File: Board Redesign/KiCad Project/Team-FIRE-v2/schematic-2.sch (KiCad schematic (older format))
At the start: 20 parts, among them J4 Conn_01x03, J5 Conn_ARM_JTAG_SWD_10, U4 TXB0108DQSR, U7 TXB0104RUT

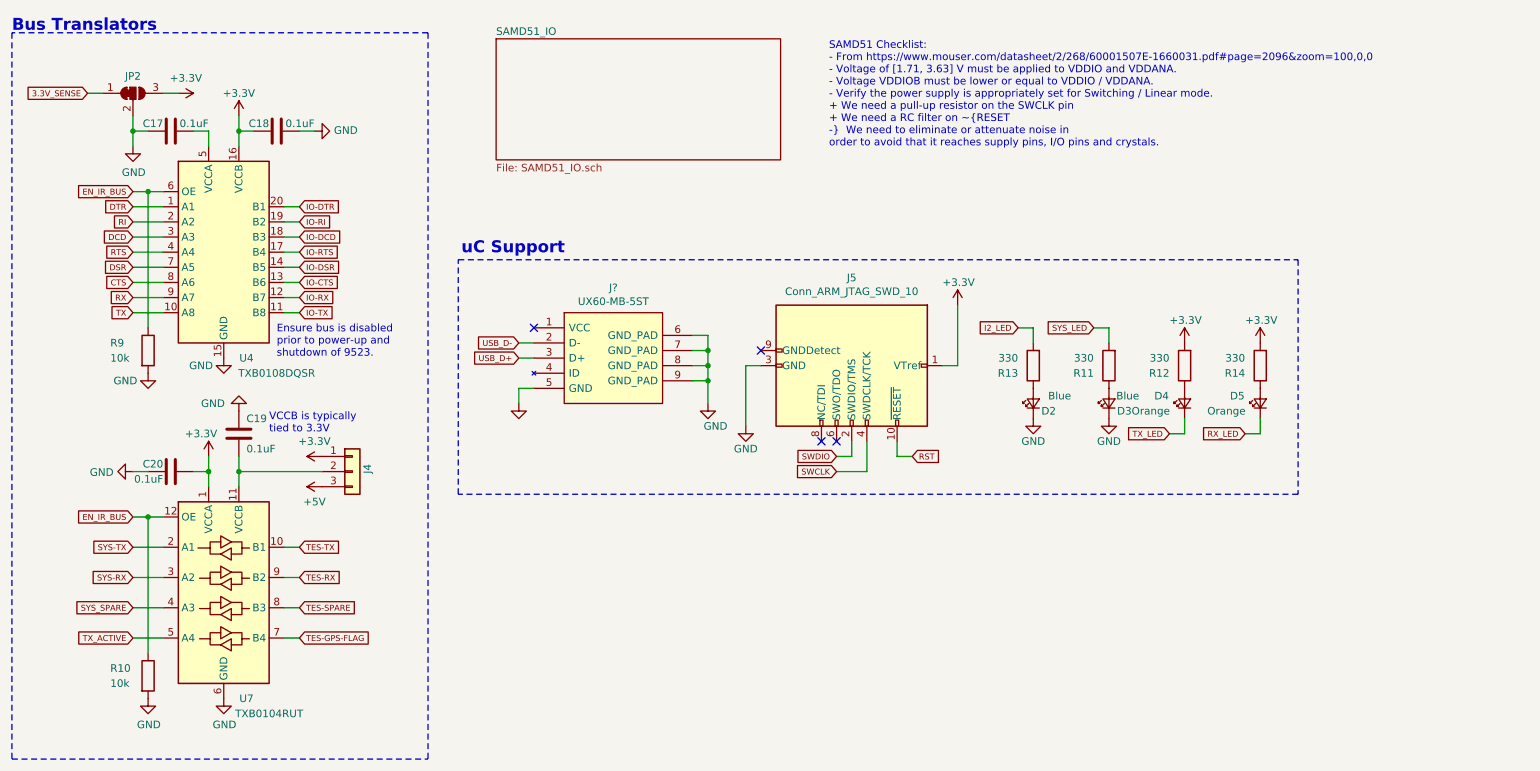
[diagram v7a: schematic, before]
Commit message: Labelled finished sections on schematic, picked LEDs
- Labelled all finished schematic sections if they've been part-selected / verified (and by whom)
- Selected the four debug LEDs and filled out BOM info
- Filled out info for Power/TES connectors
- Filled out info for RF connector
- Filled out info for 5 to 3.3V regulator
- Filled out info for 8 to 5V switching regulator
- Assigned footprints to test points
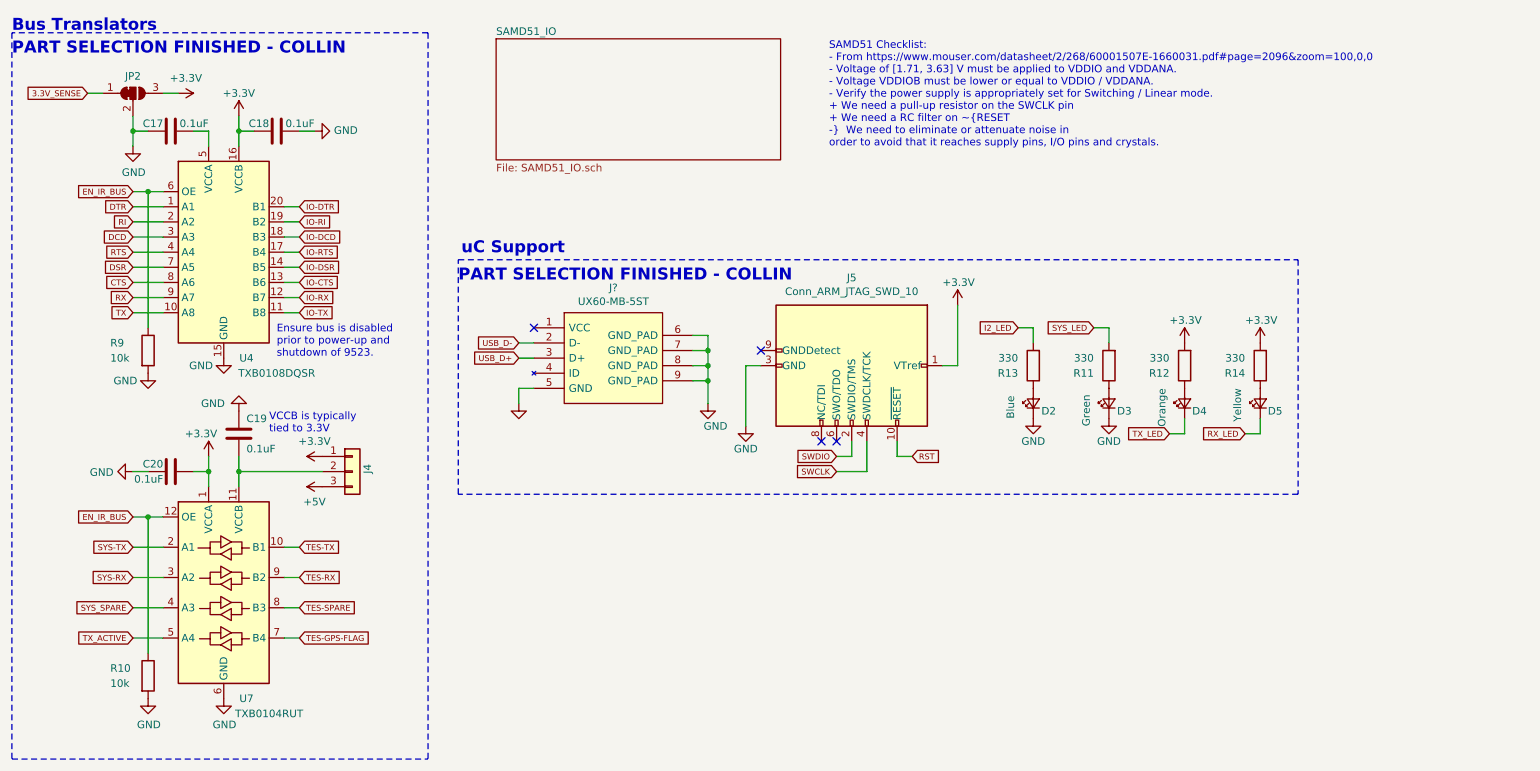
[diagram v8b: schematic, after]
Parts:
- D2: footprint (none) -> LED_SMD:LED_0603_1608Metric; Description (none) -> Blue I2 LED; Link (none) -> https://www.mouser.com/ProductDetail/OSRAM-Opto-Semiconduct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; MPN (none) -> KB DELPS2.12-QHRI-24-Z555-10-S; Manufacturer (none) -> Osram Opto Semiconductor; Supplier (none) -> Mouser; Supplier PN (none) -> 720-KBDELPS212A6350
- D3: value Blue -> Green; footprint (none) -> LED_SMD:LED_0603_1608Metric; Description (none) -> Green SYS LED; Link (none) -> https://www.mouser.com/ProductDetail/OSRAM-Opto-Semiconduct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; MPN (none) -> KG DELMS1.22-PHQI-24-E6L6; Manufacturer (none) -> Osram Opto Semiconductor; Supplier (none) -> Mouser; Supplier PN (none) -> 720-KGDELMS122A4854
- D4: footprint (none) -> LED_SMD:LED_0603_1608Metric; Description (none) -> Orange TX LED; Link (none) -> https://www.mouser.com/ProductDetail/OSRAM-Opto-Semiconduct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; MPN (none) -> KO DELLS1.22-KHLI-24; Manufacturer (none) -> Osram Opto Semiconductor; Supplier (none) -> Mouser; Supplier PN (none) -> 720-KODELLS122A4850
- D5: value Orange -> Yellow; footprint (none) -> LED_SMD:LED_0603_1608Metric; Description (none) -> Yellow RX LED; Link (none) -> https://www.mouser.com/ProductDetail/OSRAM-Opto-Semiconduct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; MPN (none) -> KY DELLS1.22-KGLH-26; Manufacturer (none) -> Osram Opto Semiconductor; Supplier (none) -> Mouser; Supplier PN (none) -> 720-KYDELLS122A4853
- J5: footprint (none) -> Connector_PinHeader_1.27mm:PinHeader_2x05_P1.27mm_Vertical_SMD; Current Rating (none) -> 3.4 A per contact; Desription (none) -> JTAG connector; Link (none) -> https://www.digikey.ca/product-detail/en/samtec-inc/FTSH-10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; MPN (none) -> FTSH-105-01-L-DV-K-TR; Manufacturer (none) -> Samtec Inc.; Supplier (none) -> Digikey; Supplier PN (none) -> SAM13165CT-ND
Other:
- note added: "PART SELECTION FINISHED - COLLIN"
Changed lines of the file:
@@
 P 7350 3150
 F 0 "D2" V 7300 3000 50  0000 L CNN
-F 1 "Blue" V 7400 2900 50  0000 L CNN
-F 2 "" V 7350 3150 50  0001 C CNN
-F 3 "~" V 7350 3150 50  0001 C CNN
+F 1 "Blue" H 7250 3300 50  0000 L CNN
+F 2 "LED_SMD:LED_0603_1608Metric" V 7350 3150 50  0001 C CNN
+F 3 "https://dammedia.osram.info/media/resource/hires/osram-dam-5455914/KB%20DELPS2.12_EN.pdf" V 7350 3150 50  0001 C CNN
+F 4 "KB DELPS2.12-QHRI-24-Z555-10-S" V 7350 3150 50  0001 C CNN "MPN"
+F 5 "Osram Opto Semiconductor" V 7350 3150 50  0001 C CNN "Manufacturer"
+F 6 "Mouser" V 7350 3150 50  0001 C CNN "Supplier"
+F 7 "720-KBDELPS212A6350" V 7350 3150 50  0001 C CNN "Supplier PN"
+F 8 "https://www.mouser.com/ProductDetail/OSRAM-Opto-Semiconductors/KB-DELPS212-QHRI-24-Z555-10-S?qs=sGAEpiMZZMseGfSY3csMkXiJOH5X%252BfXwwcjMMWonTAhZIqH765egag%3D%3D" V 7350 3150 50  0001 C CNN "Link"
+F 9 "Blue I2 LED" V 7350 3150 50  0001 C CNN "Description"
 	1    7350 3150
 	0    -1   -1   0
@@
 P 7850 3150
 F 0 "D3" V 7800 3000 50  0000 L CNN
-F 1 "Blue" V 7900 2950 50  0000 L CNN
-F 2 "" V 7850 3150 50  0001 C CNN
-F 3 "~" V 7850 3150 50  0001 C CNN
+F 1 "Green" H 7700 3300 50  0000 L CNN
+F 2 "LED_SMD:LED_0603_1608Metric" V 7850 3150 50  0001 C CNN
+F 3 "https://dammedia.osram.info/media/resource/hires/osram-dam-5667035/KG%20DELMS1.22_EN.pdf" V 7850 3150 50  0001 C CNN
+F 4 "KG DELMS1.22-PHQI-24-E6L6" V 7850 3150 50  0001 C CNN "MPN"
+F 5 "Osram Opto Semiconductor" V 7850 3150 50  0001 C CNN "Manufacturer"
+F 6 "Mouser" V 7850 3150 50  0001 C CNN "Supplier"
+F 7 "720-KGDELMS122A4854" V 7850 3150 50  0001 C CNN "Supplier PN"
+F 8 "https://www.mouser.com/ProductDetail/OSRAM-Opto-Semiconductors/KG-DELMS122-PHQI-24-E6L6?qs=sGAEpiMZZMseGfSY3csMkXiJOH5X%252BfXw2hz5dPhSTuoMKPqIbYvs3A%3D%3D" V 7850 3150 50  0001 C CNN "Link"
+F 9 "Green SYS LED" V 7850 3150 50  0001 C CNN "Description"
 	1    7850 3150
 	0    -1   -1   0
@@
 U 1 1 5E7085D2
 P 8350 3150
-F 0 "D4" V 8400 3350 50  0000 R CNN
-F 1 "Orange" V 8300 3500 50  0000 R CNN
-F 2 "" V 8350 3150 50  0001 C CNN
-F 3 "~" V 8350 3150 50  0001 C CNN
+F 0 "D4" V 8300 3100 50  0000 R CNN
+F 1 "Orange" H 8450 3300 50  0000 R CNN
+F 2 "LED_SMD:LED_0603_1608Metric" V 8350 3150 50  0001 C CNN
+F 3 "https://dammedia.osram.info/media/resource/hires/osram-dam-5667035/KG%20DELMS1.22_EN.pdf" V 8350 3150 50  0001 C CNN
+F 4 "KO DELLS1.22-KHLI-24" V 8350 3150 50  0001 C CNN "MPN"
+F 5 "Osram Opto Semiconductor" V 8350 3150 50  0001 C CNN "Manufacturer"
+F 6 "Mouser" V 8350 3150 50  0001 C CNN "Supplier"
+F 7 "720-KODELLS122A4850" V 8350 3150 50  0001 C CNN "Supplier PN"
+F 8 "https://www.mouser.com/ProductDetail/OSRAM-Opto-Semiconductors/KO-DELLS122-KHLI-24?qs=sGAEpiMZZMseGfSY3csMkXiJOH5X%252BfXw2C8037rquCtxGfEHciPG%252Bg%3D%3D" V 8350 3150 50  0001 C CNN "Link"
+F 9 "Orange TX LED" V 8350 3150 50  0001 C CNN "Description"
 	1    8350 3150
 	0    -1   -1   0
@@
 U 1 1 5E709852
 P 8850 3150
-F 0 "D5" V 8900 3350 50  0000 R CNN
-F 1 "Orange" V 8800 3500 50  0000 R CNN
-F 2 "" V 8850 3150 50  0001 C CNN
-F 3 "~" V 8850 3150 50  0001 C CNN
+F 0 "D5" V 8800 3100 50  0000 R CNN
+F 1 "Yellow" H 8950 3300 50  0000 R CNN
+F 2 "LED_SMD:LED_0603_1608Metric" V 8850 3150 50  0001 C CNN
+F 3 "https://dammedia.osram.info/media/resource/hires/osram-dam-5452388/KY%20DELLS1.22_EN.pdf" V 8850 3150 50  0001 C CNN
+F 4 "KY DELLS1.22-KGLH-26" V 8850 3150 50  0001 C CNN "MPN"
+F 5 "Osram Opto Semiconductor" V 8850 3150 50  0001 C CNN "Manufacturer"
+F 6 "Mouser" V 8850 3150 50  0001 C CNN "Supplier"
+F 7 "720-KYDELLS122A4853" V 8850 3150 50  0001 C CNN "Supplier PN"
+F 8 "https://www.mouser.com/ProductDetail/OSRAM-Opto-Semiconductors/KY-DELLS122-KGLH-26?qs=sGAEpiMZZMseGfSY3csMkXiJOH5X%252BfXwv1i%252BFa1JJszqEvno6qOTvg%3D%3D" V 8850 3150 50  0001 C CNN "Link"
+F 9 "Yellow RX LED" V 8850 3150 50  0001 C CNN "Description"
 	1    8850 3150
 	0    -1   -1   0
@@
 $EndComp
 $Comp
-L Logic_LevelTranslator:TXB0108DQSR U4
-U 1 1 5E4FCEC1
-P 2000 2150
-F 0 "U4" H 2150 1450 50  0000 C CNN
-F 1 "TXB0108DQSR" H 2350 1350 50  0000 C CNN
-F 2 "Package_SON:USON-20_2x4mm_P0.4mm" H 2000 1400 50  0001 C CNN
-F 3 "http://www.ti.com/lit/ds/symlink/txb0108.pdf" H 2000 2050 50  0001 C CNN
-F 4 "Texas Instruments" H 2000 2150 50  0001 C CNN "Manufacturer"
-F 5 "Mouser" H 2000 2150 50  0001 C CNN "Supplier"
-F 6 "595-TXB0108DQSR" H 2000 2150 50  0001 C CNN "Supplier PN"
-F 7 "https://www.mouser.com/ProductDetail/Texas-Instruments/TXB0108DQSR?qs=%2Fha2pyFadujaOGhpga6aqWJB%2FOU4nmuuEFiHYX7W5oybuilijLXCBg%3D%3D" H 2000 2150 50  0001 C CNN "Link"
-F 8 "1.2/1.65 V to 5.5 V" H 2000 2150 50  0001 C CNN "Voltage Rating"
-F 9 "Voltage bus shifter" H 2000 2150 50  0001 C CNN "Description"
-	1    2000 2150
-	1    0    0    -1
-$EndComp
-$Comp
-L Device:R R9
-U 1 1 5EB0F922
-P 1500 2800
-F 0 "R9" H 1250 2850 50  0000 L CNN
-F 1 "10k" H 1250 2750 50  0000 L CNN
-F 2 "Resistor_SMD:R_0603_1608Metric" V 1430 2800 50  0001 C CNN
-F 3 "https://www.mouser.com/datasheet/2/427/mcx0x0xpre-1762843.pdf" H 1500 2800 50  0001 C CNN
-F 4 "MCT06030E1002BP100" H 1500 2800 50  0001 C CNN "MPN"
-F 5 "Vishay" H 1500 2800 50  0001 C CNN "Manufacturer"
-F 6 "Mouser" H 1500 2800 50  0001 C CNN "Supplier"
-F 7 "594-MCT06030E1002BP1" H 1500 2800 50  0001 C CNN "Supplier PN"
-F 8 "https://www.mouser.com/ProductDetail/Vishay-Beyschlag/MCT06030E1002BP100?qs=sGAEpiMZZMtlubZbdhIBIHIEm3drdiPa32EPxwxqfD0%3D" H 1500 2800 50  0001 C CNN "Link"
-F 9 "Thin Film Resistor" H 1500 2800 50  0001 C CNN "Type"
-F 10 "0.1%" H 1500 2800 50  0001 C CNN "Tolerance"
-F 11 "75 V" H 1500 2800 50  0001 C CNN "Voltage Rating"
-	1    1500 2800
-	1    0    0    -1
-$EndComp
-$Comp
 L Device:C C?
 U 1 1 5EB1A931
@@
 F 0 "J5" V 5569 2900 50  0000 C CNN
 F 1 "Conn_ARM_JTAG_SWD_10" V 5660 2900 50  0000 C CNN
-F 2 "" H 6150 2900 50  0001 C CNN
+F 2 "Connector_PinHeader_1.27mm:PinHeader_2x05_P1.27mm_Vertical_SMD" H 6150 2900 50  0001 C CNN
 F 3 "http://infocenter.arm.com/help/topic/com.arm.doc.ddi0314h/DDI0314H_coresight_components_trm.pdf" V 5800 1650 50  0001 C CNN
+F 4 "FTSH-105-01-L-DV-K-TR" V 6150 2900 50  0001 C CNN "MPN"
+F 5 "Samtec Inc." V 6150 2900 50  0001 C CNN "Manufacturer"
+F 6 "Digikey" V 6150 2900 50  0001 C CNN "Supplier"
+F 7 "SAM13165CT-ND" V 6150 2900 50  0001 C CNN "Supplier PN"
+F 8 "https://www.digikey.ca/product-detail/en/samtec-inc/FTSH-105-01-L-DV-K-TR/SAM13165CT-ND/8827920" V 6150 2900 50  0001 C CNN "Link"
+F 9 "3.4 A per contact" V 6150 2900 50  0001 C CNN "Current Rating"
+F 10 "JTAG connector" V 6150 2900 50  0001 C CNN "Desription"
 	1    6150 2900
 	0    1    1    0
@@
 Wire Wire Line
 	6450 3400 6450 3500
+Text Notes 3550 2350 0    79   ~ 16
+PART SELECTION FINISHED - COLLIN
+Text Notes 600  850  0    79   ~ 16
+PART SELECTION FINISHED - COLLIN
+$Comp
+L Device:R R9
+U 1 1 5EB0F922
+P 1500 2800
+F 0 "R9" H 1250 2850 50  0000 L CNN
+F 1 "10k" H 1250 2750 50  0000 L CNN
+F 2 "Resistor_SMD:R_0603_1608Metric" V 1430 2800 50  0001 C CNN
+F 3 "https://www.mouser.com/datasheet/2/427/mcx0x0xpre-1762843.pdf" H 1500 2800 50  0001 C CNN
+F 4 "MCT06030E1002BP100" H 1500 2800 50  0001 C CNN "MPN"
+F 5 "Vishay" H 1500 2800 50  0001 C CNN "Manufacturer"
+F 6 "Mouser" H 1500 2800 50  0001 C CNN "Supplier"
+F 7 "594-MCT06030E1002BP1" H 1500 2800 50  0001 C CNN "Supplier PN"
+F 8 "https://www.mouser.com/ProductDetail/Vishay-Beyschlag/MCT06030E1002BP100?qs=sGAEpiMZZMtlubZbdhIBIHIEm3drdiPa32EPxwxqfD0%3D" H 1500 2800 50  0001 C CNN "Link"
+F 9 "Thin Film Resistor" H 1500 2800 50  0001 C CNN "Type"
+F 10 "0.1%" H 1500 2800 50  0001 C CNN "Tolerance"
+F 11 "75 V" H 1500 2800 50  0001 C CNN "Voltage Rating"
+	1    1500 2800
+	1    0    0    -1
+$EndComp
+$Comp
+L Logic_LevelTranslator:TXB0108DQSR U4
+U 1 1 5E4FCEC1
+P 2000 2150
+F 0 "U4" H 2150 1450 50  0000 C CNN
+F 1 "TXB0108DQSR" H 2350 1350 50  0000 C CNN
+F 2 "Package_SON:USON-20_2x4mm_P0.4mm" H 2000 1400 50  0001 C CNN
+F 3 "http://www.ti.com/lit/ds/symlink/txb0108.pdf" H 2000 2050 50  0001 C CNN
+F 4 "Texas Instruments" H 2000 2150 50  0001 C CNN "Manufacturer"
+F 5 "Mouser" H 2000 2150 50  0001 C CNN "Supplier"
+F 6 "595-TXB0108DQSR" H 2000 2150 50  0001 C CNN "Supplier PN"
+F 7 "https://www.mouser.com/ProductDetail/Texas-Instruments/TXB0108DQSR?qs=%2Fha2pyFadujaOGhpga6aqWJB%2FOU4nmuuEFiHYX7W5oybuilijLXCBg%3D%3D" H 2000 2150 50  0001 C CNN "Link"
+F 8 "1.2/1.65 V to 5.5 V" H 2000 2150 50  0001 C CNN "Voltage Rating"
+F 9 "Voltage bus shifter" H 2000 2150 50  0001 C CNN "Description"
+	1    2000 2150
+	1    0    0    -1
+$EndComp
 $EndSCHEMATC
